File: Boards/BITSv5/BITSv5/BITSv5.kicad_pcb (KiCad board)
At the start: 4 copper layers, 47 x 45 mm, 100 parts, among them J1 Conn_01x03_Pin, J2 USB_C_Receptacle_USB2.0, J3 SOICbite, J4 Conn_01x10_Pin, J5 U.FL, J6 U.FL, Q1 Q_NMOS_GSD, SW3 SLIDE, U1 MCU_RaspberryPi_RP2040_RP2040, U10 USBLC6-2SC6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

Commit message: BITSv5.1 ready for review
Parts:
- added C30: 100nF, Capacitor_SMD:C_0603_1608Metric, F.Cu at (141.3, 75.3)
- added U7: MB85RS1MT, BPP_Lib:BGA8CP30X40_5X3_309X228X35B25N, F.Cu at (138.1, 76.4)
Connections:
- net /DRF_CLK renamed /SCK
- net /DRF_MISO renamed /MISO
- net /DRF_MOSI renamed /MOSI
- BT1 pad 1: +BATT -> GND
- BT1 pad 2: GND -> +BATT
- U1 pad 41: unconnected-(U1-GPIO29_ADC3-Pad41) -> /FRAM_CS
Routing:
- net /FRAM_CS: track 0.00 -> 28.8 mm, vias 0 -> 3
- net /MISO: track 18.9 -> 33.3 mm, vias 1 -> 3
- net /MOSI: track 22.9 -> 30.1 mm, vias 1 -> 3
- net /SCK: track 23.7 -> 29.7 mm, vias 1 -> 3
- net +3V3: track 68.0 -> 72.8 mm, vias 26 -> 27
- net GND: track 112.9 -> 108.4 mm, vias 170 -> 171
- net /DRF_CS: track 22.9 -> 21.3 mm
- net /DRF_TXEN: track 9.34 -> 10.5 mm
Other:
- board text added: "BITSv5.1 01/2024"
- board text added: "J. Bishop M. Shipman"
- board text added: "ON"
- board text removed: "BITSv5.0 10/2023"
- board text removed: "J. Bishop M. Shipman A. Takeuchi"

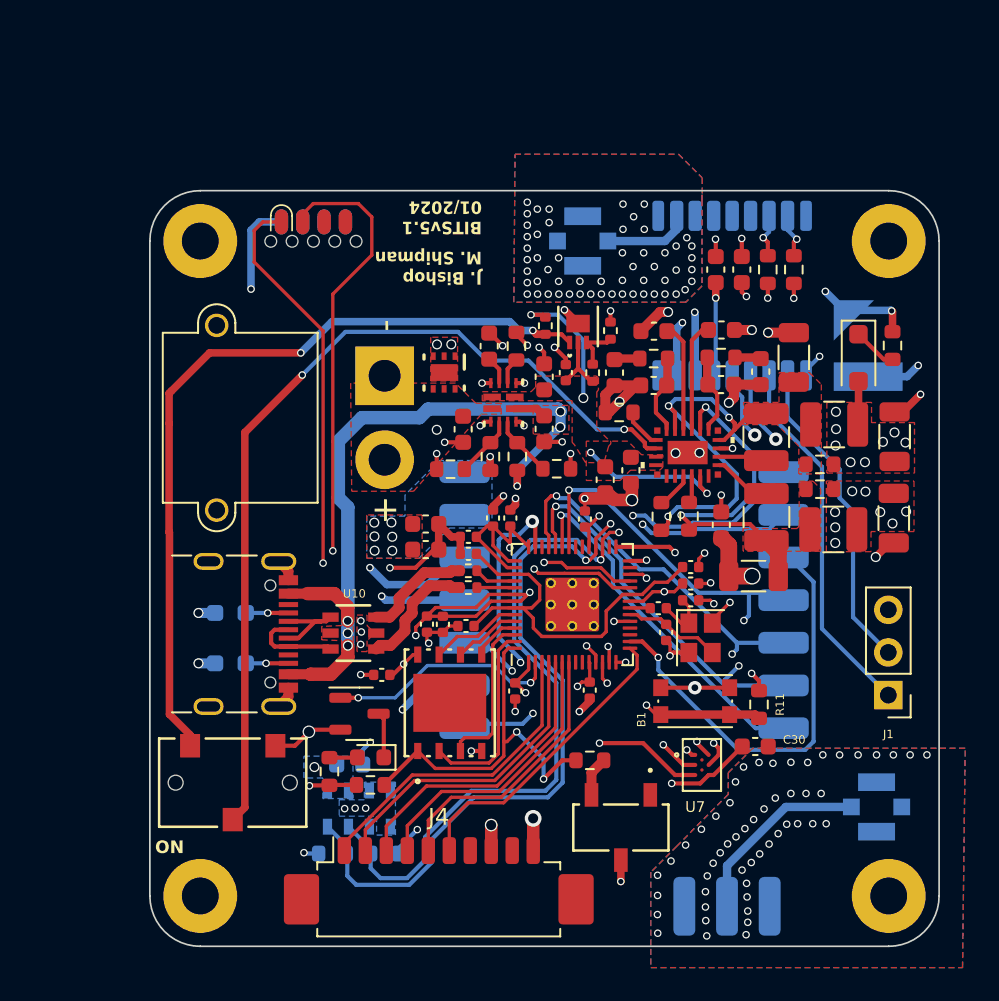
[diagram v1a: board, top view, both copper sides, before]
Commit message: nvm I want BITSv5 to have a chip antenna
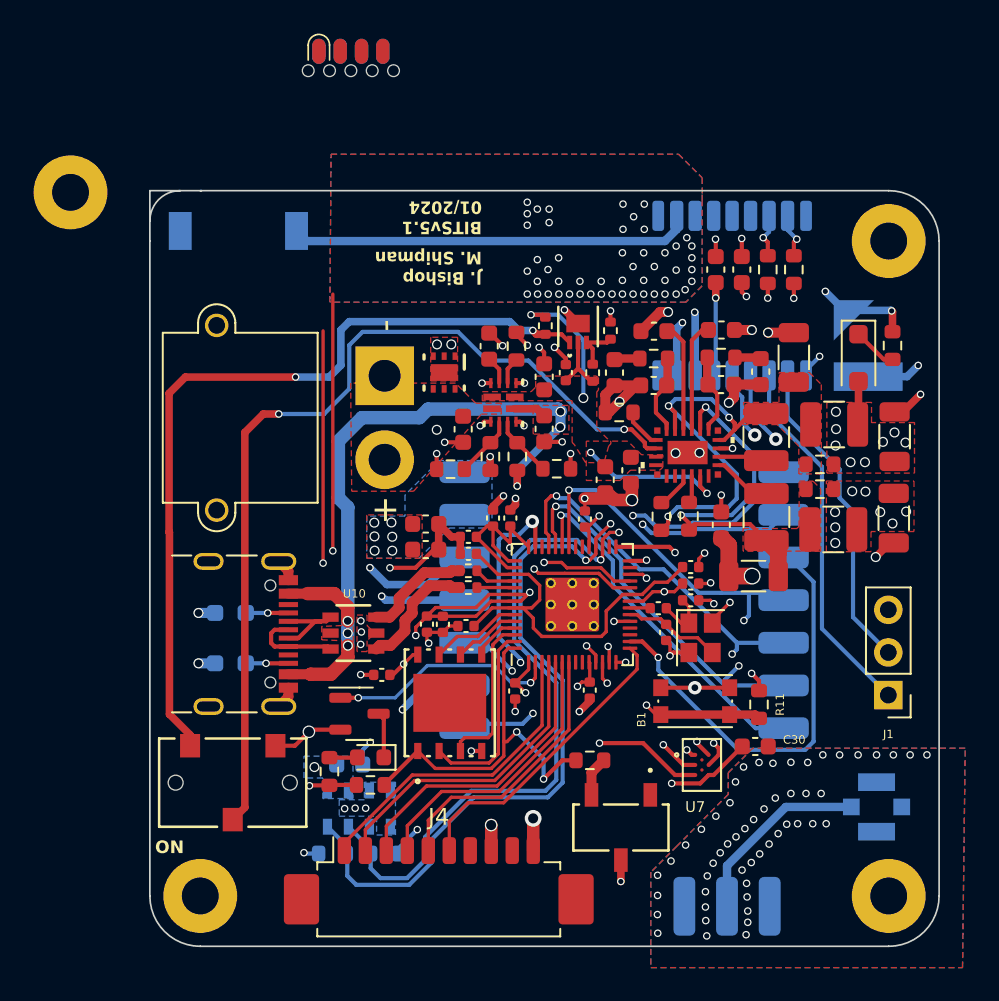
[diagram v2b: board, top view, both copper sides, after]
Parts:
- removed J5: U.FL, Connector_Coaxial:U.FL_Molex_MCRF_73412-0110_Vertical
- added AE1: Antenna, BPP_Lib:ANT_1575AT_JOT-M, B.Cu at (110.5, 44.6)
- moved J3 10.4 mm to (117.2, 33.1)
- moved H1 8.25 mm to (100.5, 42.3)
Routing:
- net Net-(AE1-A): track 5.19 -> 24.0 mm
- net /RP_SWD: track 45.3 -> 34.6 mm
- net /RP_SWCLK: track 43.0 -> 33.5 mm
- net GND: track 108.4 -> 102.9 mm, vias 171 -> 165
- net /LVC_CUTOFF: track 53.3 -> 54.8 mm
- net Net-(SW3-C): track 47.6 -> 48.9 mm
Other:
- outline, holes or cut-outs redrawn

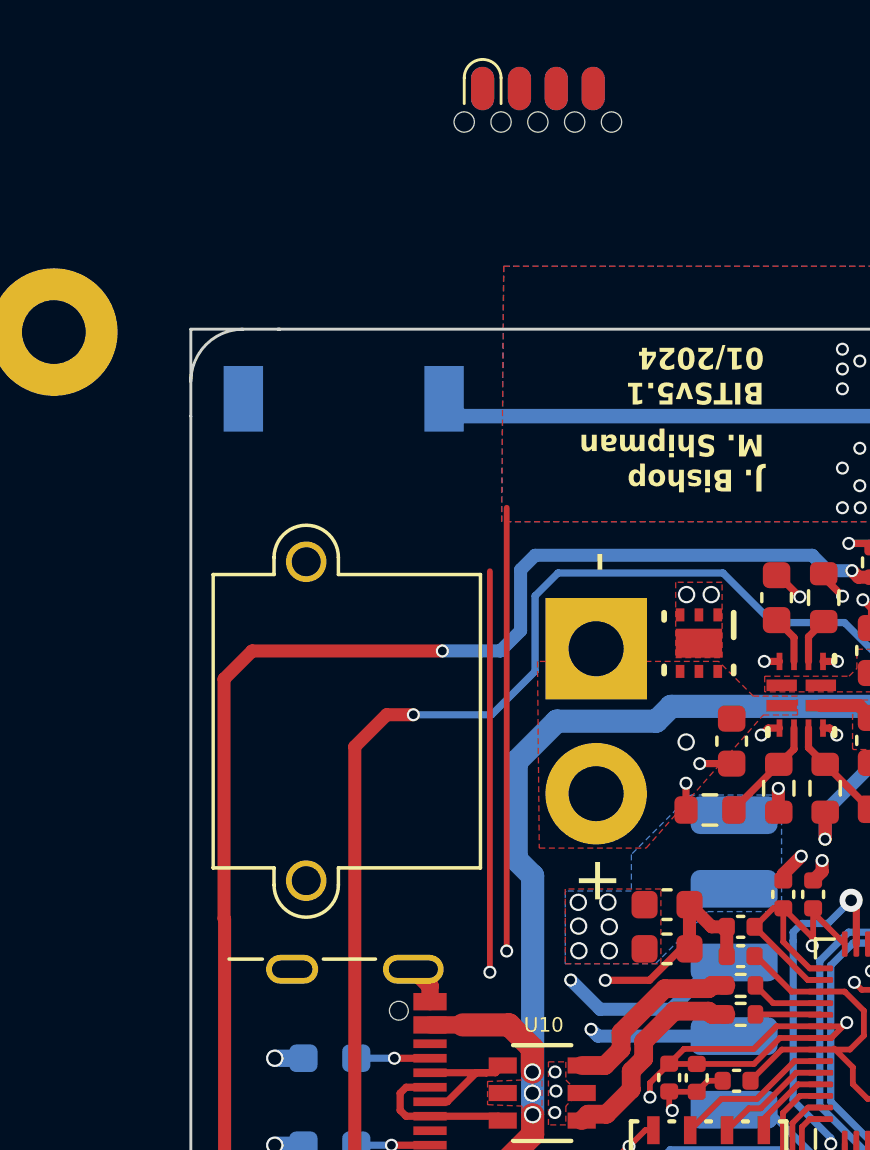
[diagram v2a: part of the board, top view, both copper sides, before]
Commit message: finished GPS chip antenna, removed SOICbite for test points because couldn't find space
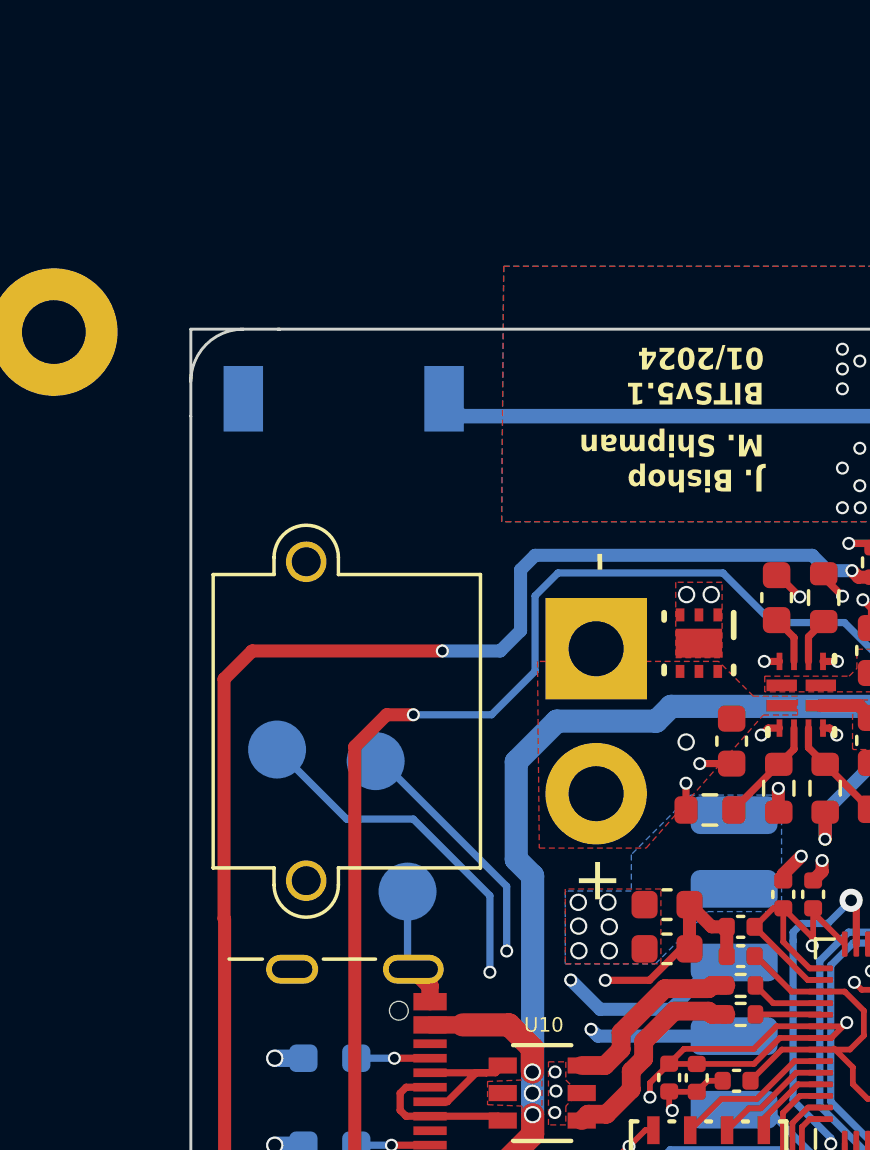
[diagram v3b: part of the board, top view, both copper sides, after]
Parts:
- removed J3: SOICbite, BITSv5:SOIC_clipProgSmall
- added TP1: TestPoint, TestPoint:TestPoint_Pad_D2.0mm, B.Cu at (108.2, 56.7)
- added TP2: TestPoint, TestPoint:TestPoint_Pad_D2.0mm, B.Cu at (111.6, 57.1)
- added TP3: TestPoint, TestPoint:TestPoint_Pad_D2.0mm, B.Cu at (112.7, 61.6)
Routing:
- net /RP_SWD: track 34.6 -> 27.8 mm
- net GND: track 102.9 -> 105.6 mm
- net /RP_SWCLK: track 33.5 -> 32.0 mm

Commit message: clean up
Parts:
- removed H1: M2, MountingHole:MountingHole_2.2mm_M2_Pad
- moved AE1 0.86 mm to (111.2, 44.1)
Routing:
- net Net-(SW3-C): track 48.9 -> 48.5 mm, vias 2 -> 3
- net GND: vias 165 -> 148
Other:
- outline, holes or cut-outs redrawn

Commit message: BITSv5.1 ready for order, Gerbers generated
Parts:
- added REF**: BalloonArt, BPP_Lib:BalloonArt, F.Cu at (148.7, 79.1)
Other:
- board text added: "BITSv5.1 02/2024"
- board text added: "JLCJLCJLCJLC"
- board text removed: "BITSv5.1 01/2024"
